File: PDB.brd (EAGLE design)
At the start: 160 x 100 mm, 31 parts, among them J1_CONNECTOR_INPUT 5566-4, U1 MICROCHIP_MIC29300-3_3WUMICRO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, U2 MIC29300-5.0WU-TR

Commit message: wiring complete
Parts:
- moved U2 57.3 mm to (63.5, 73.7)
- moved CPU_BOARD 53.5 mm to (90.2, 40.6)
- moved ENCODER 53.5 mm to (90.2, 73.7)
- moved LIDAR 53.5 mm to (90.2, 24.1)
- moved MOTOR 53.5 mm to (90.2, 86.4)
- moved WIFI 53.5 mm to (90.2, 57.1)
- moved FUSE_3 47.3 mm to (61.0, 53.3), turned to 180 degrees
- moved D2 18.2 mm to (74.9, 61.0), turned to 180 degrees
- moved CR1 15.3 mm to (72.4, 27.9)
- moved U$1 13.3 mm to (72.4, 49.5), turned to 180 degrees
- moved R2 12.0 mm to (47.0, 53.3)
- moved R1 12.0 mm to (47.0, 45.7)
- moved R3 12.0 mm to (47.0, 61.0)
- moved R4 12.0 mm to (47.0, 68.6)
- moved FUSE_1 10.2 mm to (61.0, 45.7), turned to 180 degrees
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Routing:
- net GND: track 292.1 -> 452.9 mm
- net N$3: track 75.0 -> 199.9 mm
- net 24V_RAIL: track 167.4 -> 276.2 mm
- net N$6: track 96.2 -> 156.1 mm
- net N$5: track 141.1 -> 189.5 mm
- net N$7: track 95.7 -> 60.5 mm
- net N$1: track 77.1 -> 91.8 mm
- net N$10: track 27.5 -> 38.2 mm
- net N$8: track 26.4 -> 34.2 mm
- net N$2: track 41.7 -> 47.7 mm
- net 2_GND: track 0.00 -> 3.89 mm
- net N$9: track 40.9 -> 44.5 mm
- net N$4: track 102.5 -> 100.5 mm

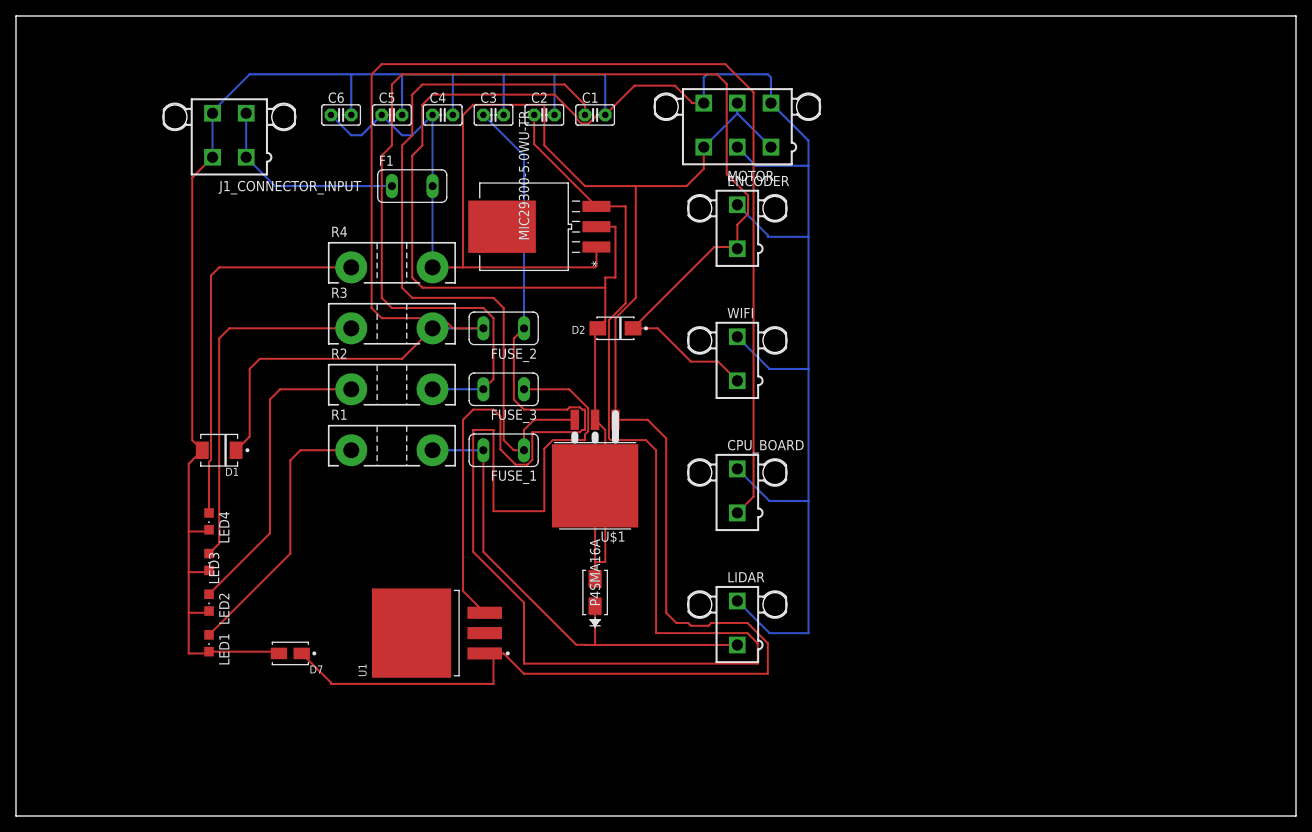
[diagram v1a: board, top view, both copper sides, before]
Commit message: Updated MIC2930 linear regulators to all use the same symbol and footprint. Fixed all warnings and errors with schematic and board.
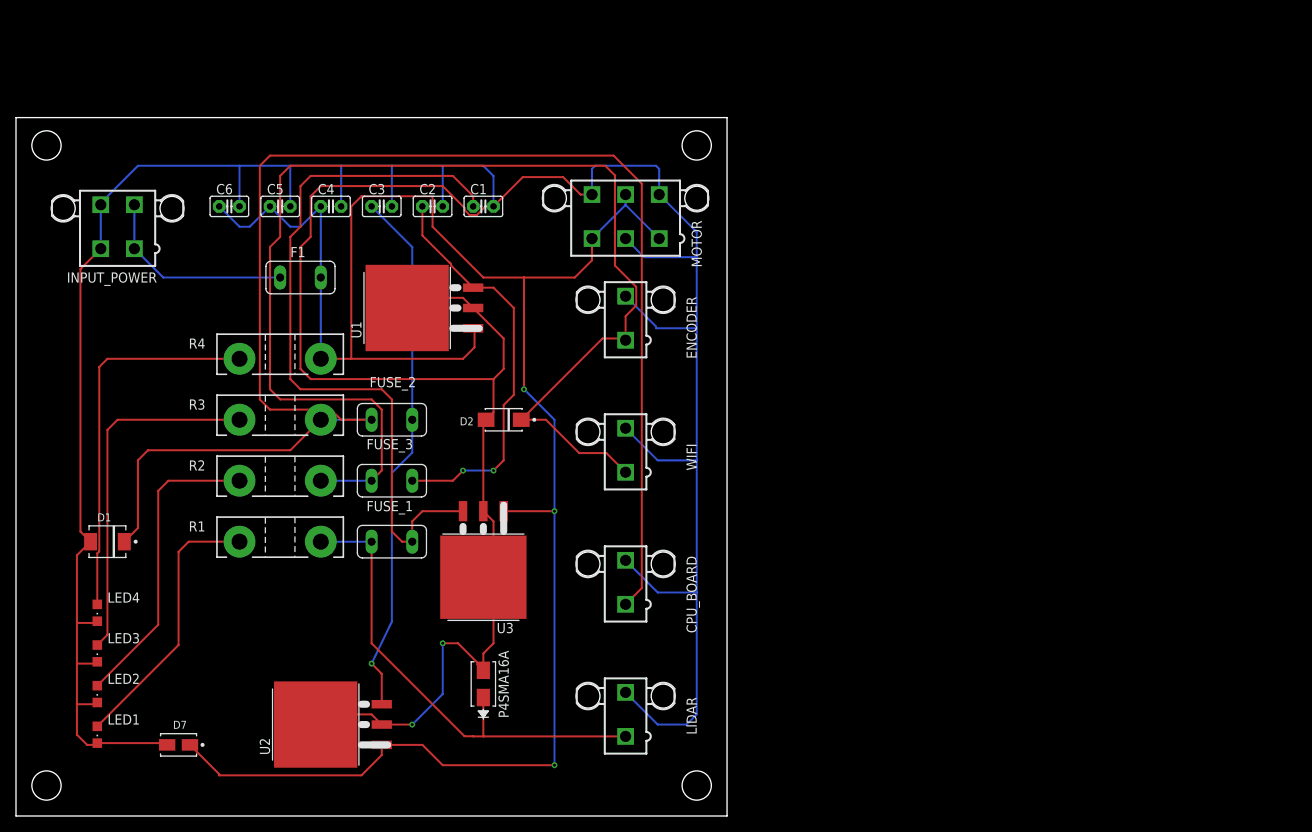
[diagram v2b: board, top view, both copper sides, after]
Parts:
- removed J1_CONNECTOR_INPUT: 5566-4, con-molex:5566-4
- removed U$1: MIC29300-12WU, MIC29300-12WU:TO263
- added INPUT_POWER: 5566-4, con-molex:5566-4
- added U3: MIC29300-12WU, MIC29300:TO263
- LED1: value (none) -> 12 V
- LED2: value (none) -> 5 V
- LED3: value (none) -> 3.3 V
- LED4: value (none) -> 24 V
- R4: value (none) -> 1K
- U1: value MICROCHIP_MIC29300-3_3WUMICROCHIP_MIC29300-3_3WU_0_0 -> MIC29300-5WU; device Microchip - MIC29300-3.3WU:MICROCHIP_MIC29300-3_3WU_0 -> MIC29300:TO263
- U2: value MIC29300-5.0WU-TR -> MIC29300-3.3WU; device mic29300-5v:TO-263-3_MCH -> MIC29300:TO263
- moved U2 64.7 mm to (45.7, 11.4)
- moved U1 41.1 mm to (57.1, 63.5)
- moved D2 18.1 mm to (61.0, 49.5)
- moved FUSE_3 18.1 mm to (47.0, 41.9)
- moved R2 18.1 mm to (33.0, 41.9)
- moved C2 18.1 mm to (52.1, 76.2)
- moved C4 18.1 mm to (39.4, 76.2)
- moved CPU_BOARD 18.1 mm to (76.2, 29.2)
- moved CR1 18.1 mm to (58.4, 16.5)
- moved D1 18.1 mm to (11.4, 34.3)
- moved D7 18.1 mm to (20.3, 8.89)
- moved ENCODER 18.1 mm to (76.2, 62.2)
- moved FUSE_1 18.1 mm to (47.0, 34.3)
- moved FUSE_2 18.1 mm to (47.0, 49.5)
- moved LED1 18.1 mm to (10.2, 10.2)
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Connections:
- removed net 1_GND: U1.2
- removed net 2_GND: U1.4
- net 24V_RAIL: now also U3.1; no longer U$1.1
- net GND: now also INPUT_POWER.2, INPUT_POWER.4, U1.2, U1.GND@, U2.GND@, U3.2, U3.GND@; no longer J1_CONNECTOR_INPUT.2, J1_CONNECTOR_INPUT.4, U$1.2, U$1.GND@
- net N$1: now also U3.3; no longer U$1.3
- net N$3: now also U1.3; no longer U2.3
- net N$4: now also U2.3; no longer U1.3
- net VCC: now also INPUT_POWER.1, INPUT_POWER.3; no longer J1_CONNECTOR_INPUT.1, J1_CONNECTOR_INPUT.3
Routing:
- net N$3: track 199.9 -> 51.0 mm, vias 0 -> 2
- net N$4: track 100.5 -> 66.5 mm, vias 0 -> 1
- net GND: track 452.9 -> 482.8 mm, vias 0 -> 2
- net 24V_RAIL: track 276.2 -> 250.6 mm, vias 0 -> 3
- net 2_GND: track 3.89 -> 0.00 mm
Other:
- board size 160 x 100 mm -> 88.9 x 87.3 mm
